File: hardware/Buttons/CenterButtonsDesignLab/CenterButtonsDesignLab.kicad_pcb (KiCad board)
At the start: 2 copper layers, 20 x 110 mm, 6 parts, among them J1 Conn_01x01, J2 Conn_01x01, J3 Conn_01x03, SW1 SW_Push, SW2 SW_Push, SW3 SW_Push

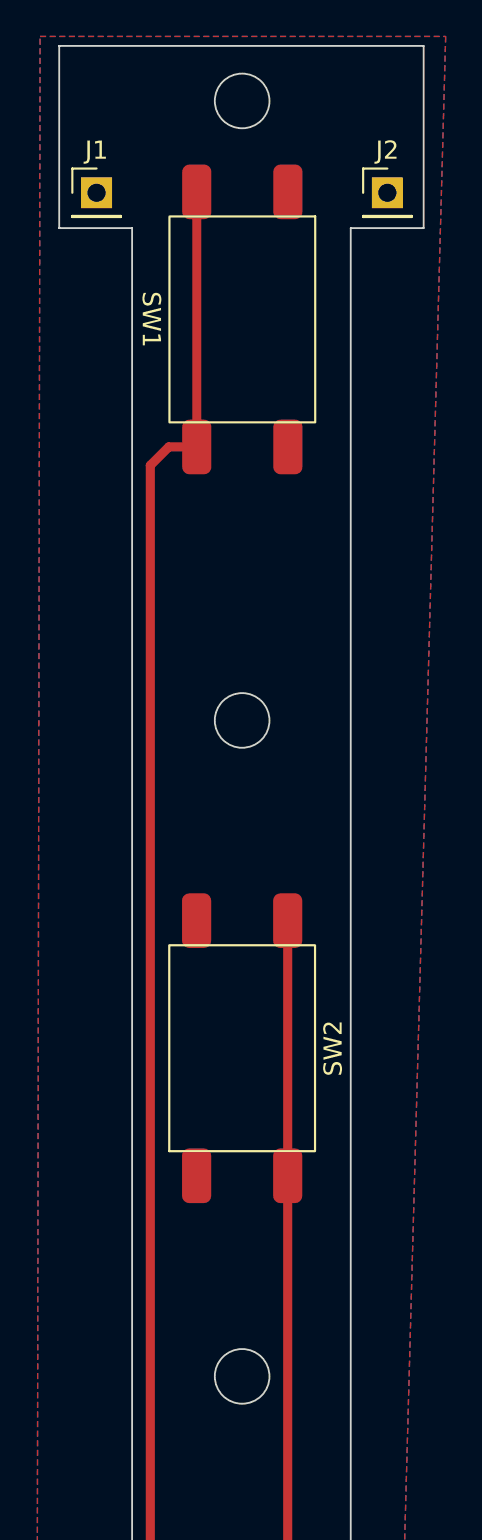
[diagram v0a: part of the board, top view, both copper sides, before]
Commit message: update labels buttons
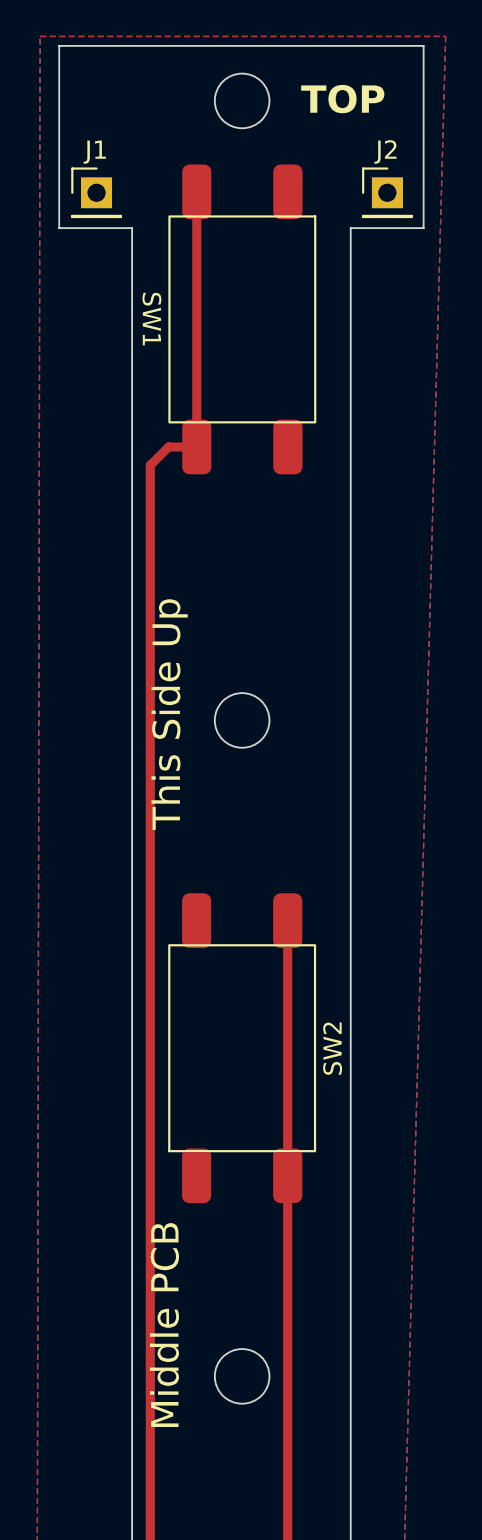
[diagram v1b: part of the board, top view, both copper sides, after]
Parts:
- added G***: LOGO, LOGO, B.Cu at (130.1, 86.2)
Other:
- board text added: "Middle PCB"
- board text added: "TOP"
- board text added: "This Side Up"

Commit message: Update labels
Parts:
- removed G***: LOGO, LOGO
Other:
- board text added: "This side up >"
- board text removed: "This Side Up"

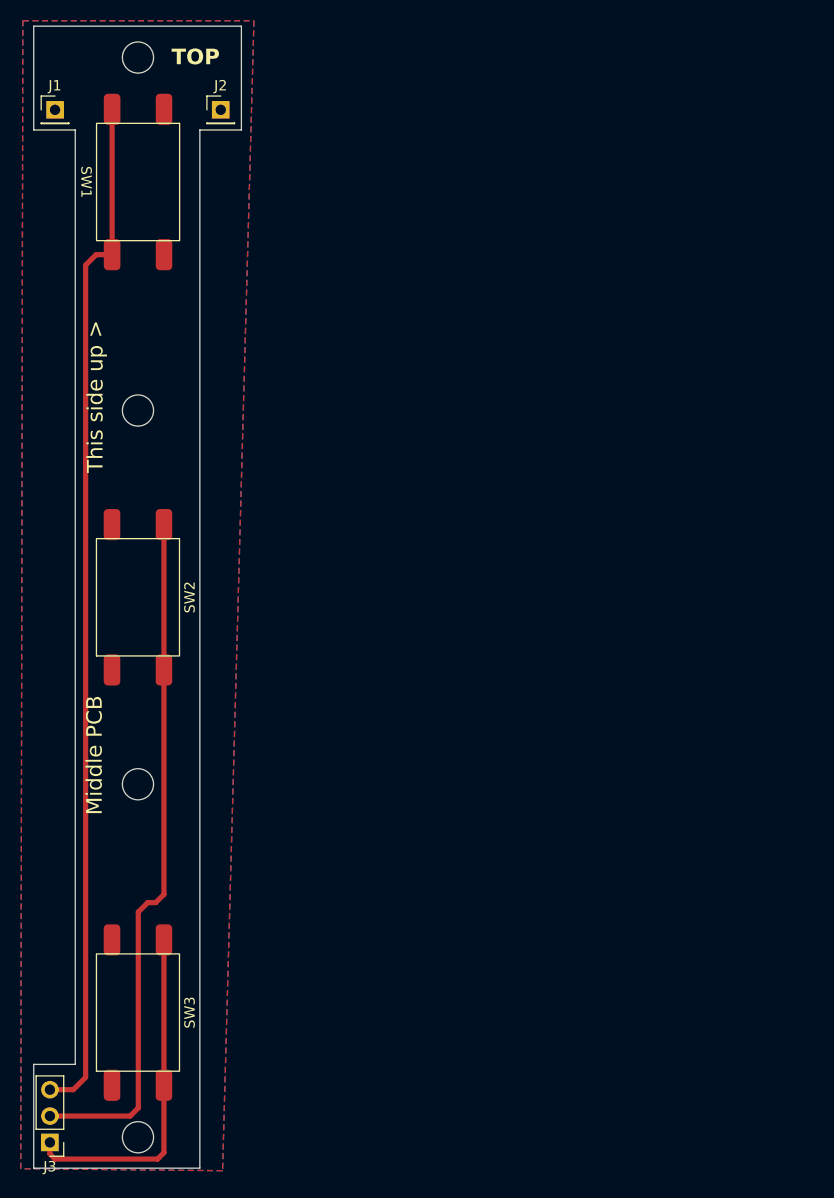
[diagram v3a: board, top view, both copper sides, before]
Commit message: PCB of the middle buttons changed
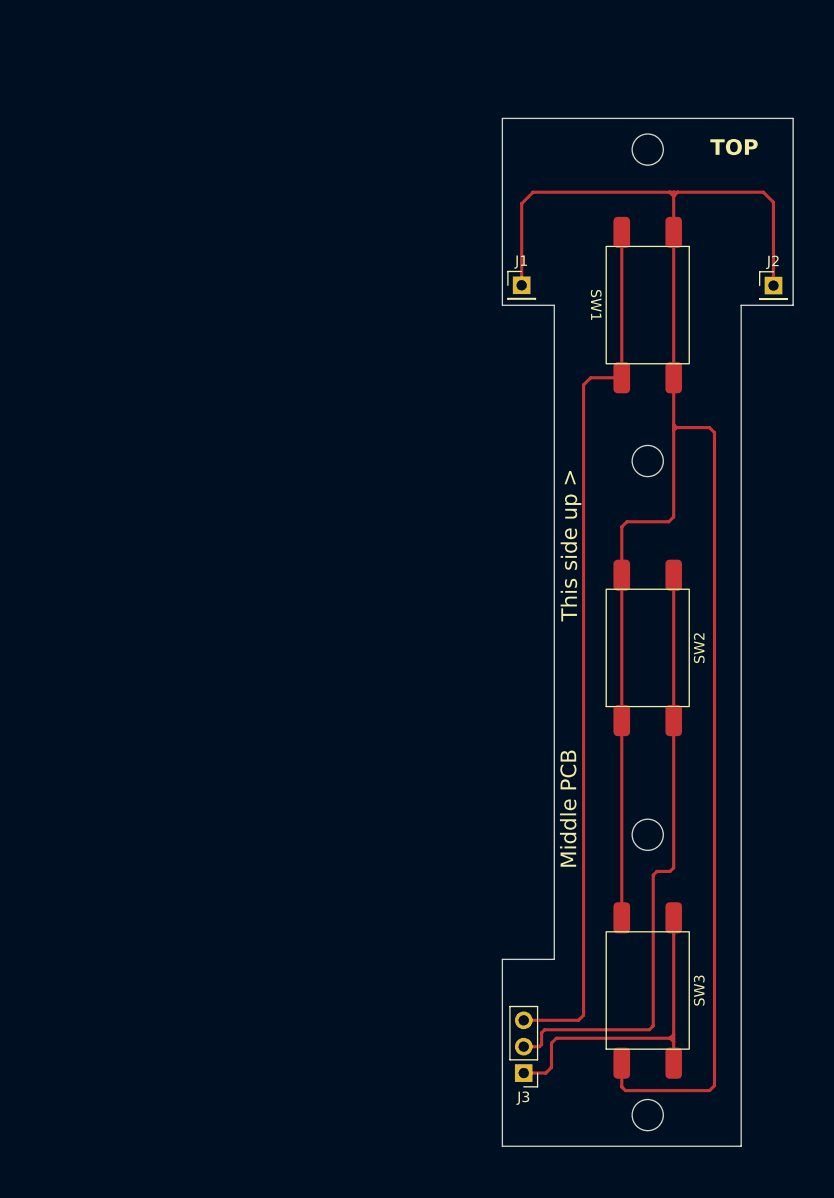
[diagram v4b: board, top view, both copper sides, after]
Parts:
- moved J2 55.9 mm to (191.3, 56.1)
- moved SW1 50.5 mm to (179.2, 58.0)
- moved SW2 49.3 mm to (179.2, 91.0)
- moved SW3 49.1 mm to (179.2, 124.0)
- moved J1 48.0 mm to (167.0, 56.1)
- moved J3 46.1 mm to (167.2, 132.0)
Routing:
- net /GND: track 0.00 -> 195.8 mm
- net /D1: track 99.1 -> 84.6 mm
- net /D4: track 66.5 -> 59.2 mm
- net /D7: track 33.0 -> 32.3 mm
- removed copper zone on B.Cu, net /GND
- removed copper zone on F.Cu, net /GND
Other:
- board size 20 x 110 mm -> 28 x 99 mm

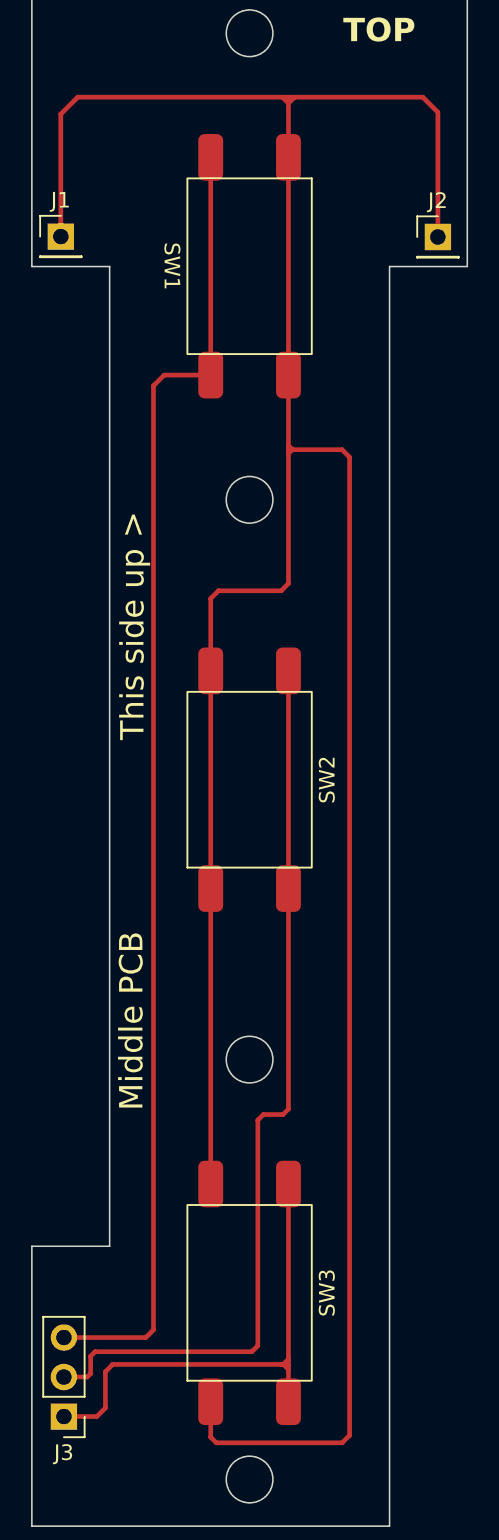
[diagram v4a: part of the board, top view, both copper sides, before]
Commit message: Changed PCB of central buttons
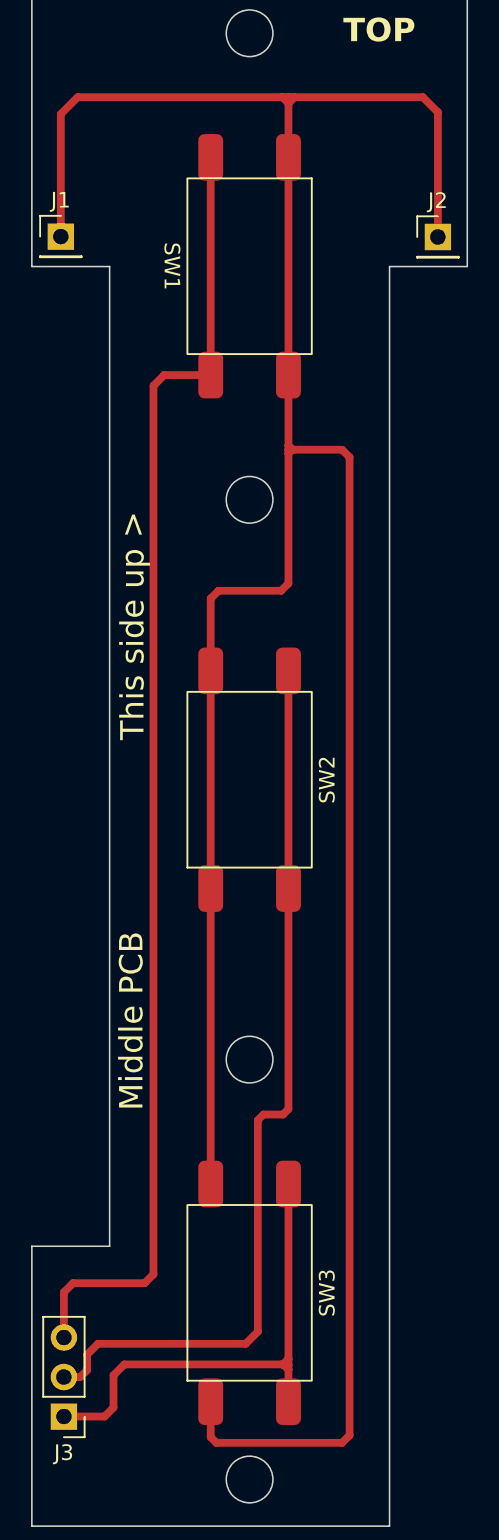
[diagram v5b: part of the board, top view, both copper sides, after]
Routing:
- net /D4: track 59.2 -> 58.3 mm

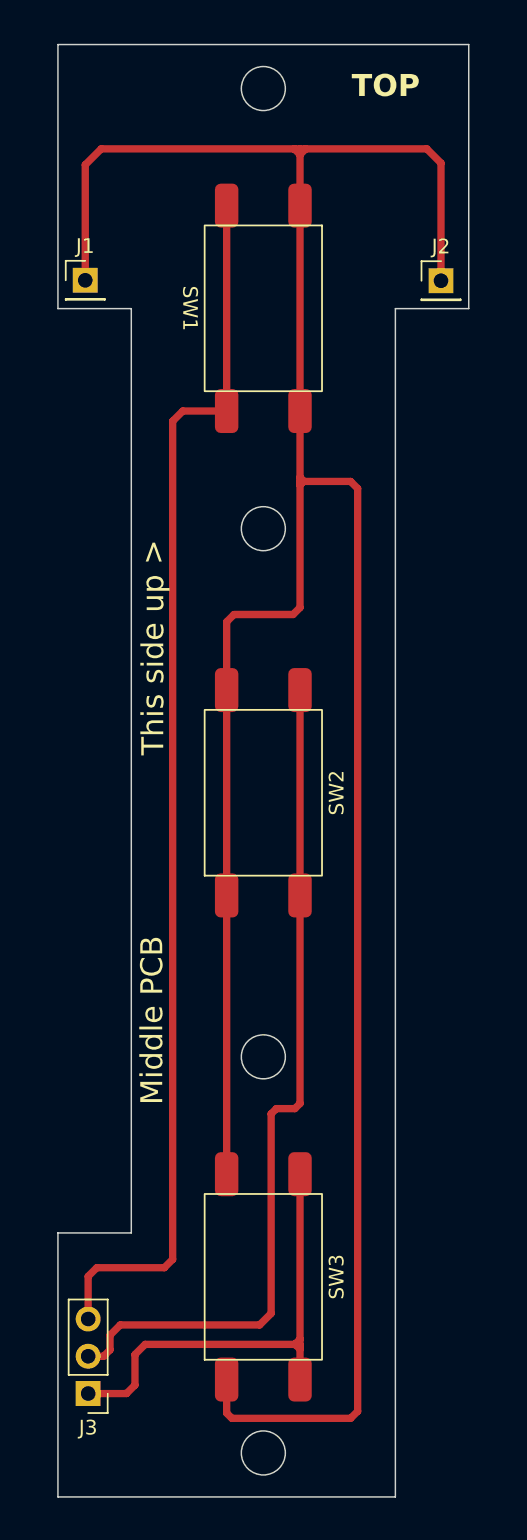
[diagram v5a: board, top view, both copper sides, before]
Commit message: SD, USB and labels changed
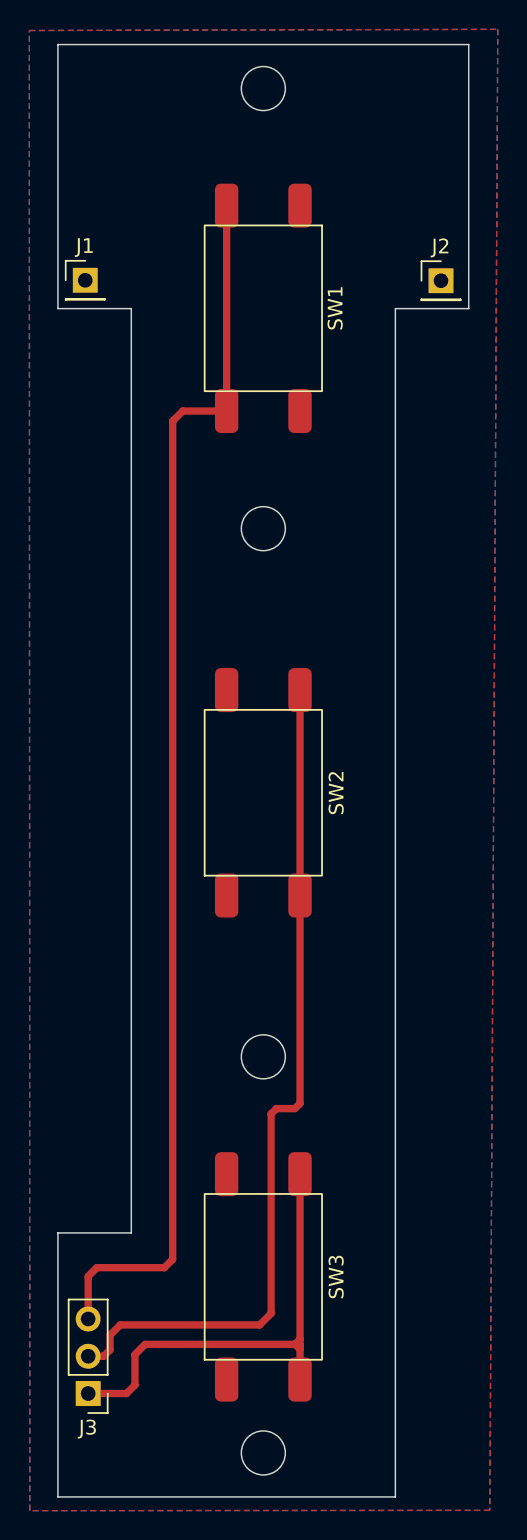
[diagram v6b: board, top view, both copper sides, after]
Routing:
- net /GND: track 195.8 -> 0.00 mm
- added copper zone on B.Cu, net /GND
- added copper zone on F.Cu, net /GND
